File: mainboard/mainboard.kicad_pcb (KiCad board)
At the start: 2 copper layers, 3 parts, among them J1 USB_B_Micro, U1 SX1276, U3 ATtiny85V-10M

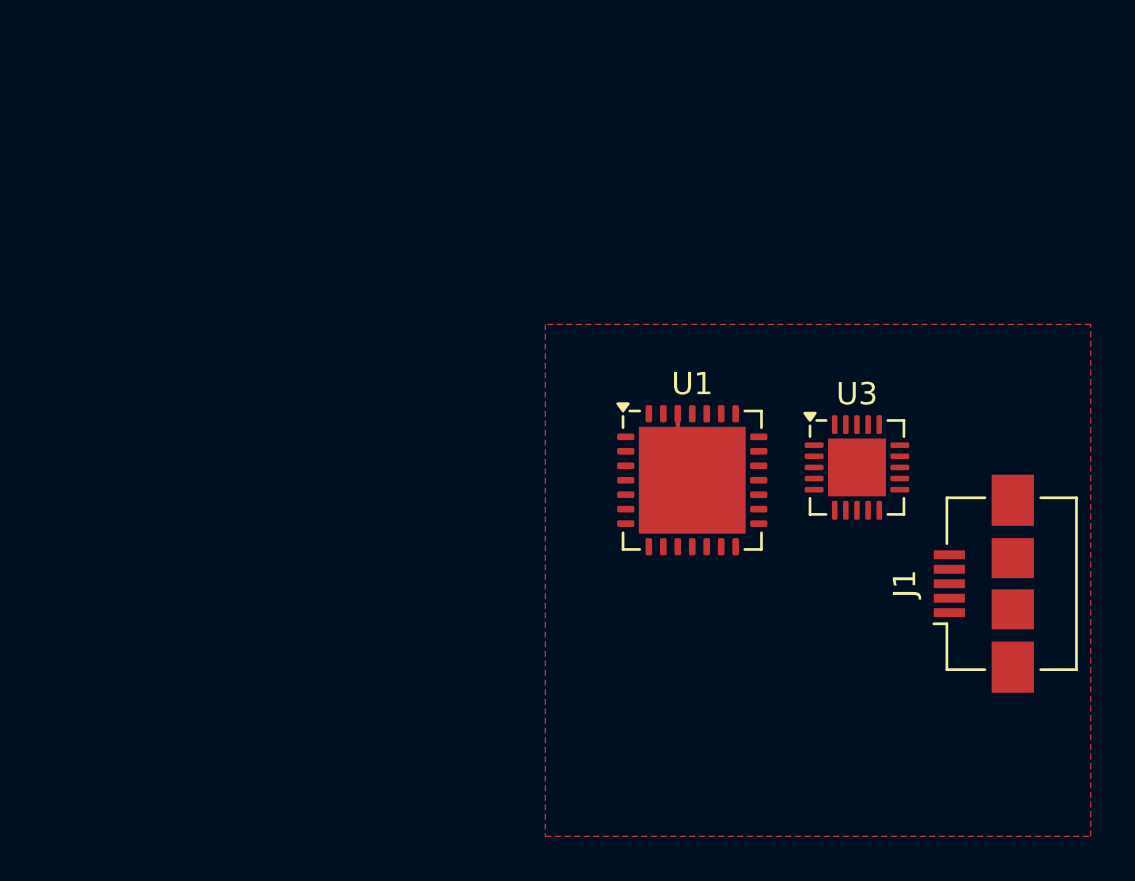
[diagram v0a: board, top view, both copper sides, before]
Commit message: Updated mainboard, and schematics.
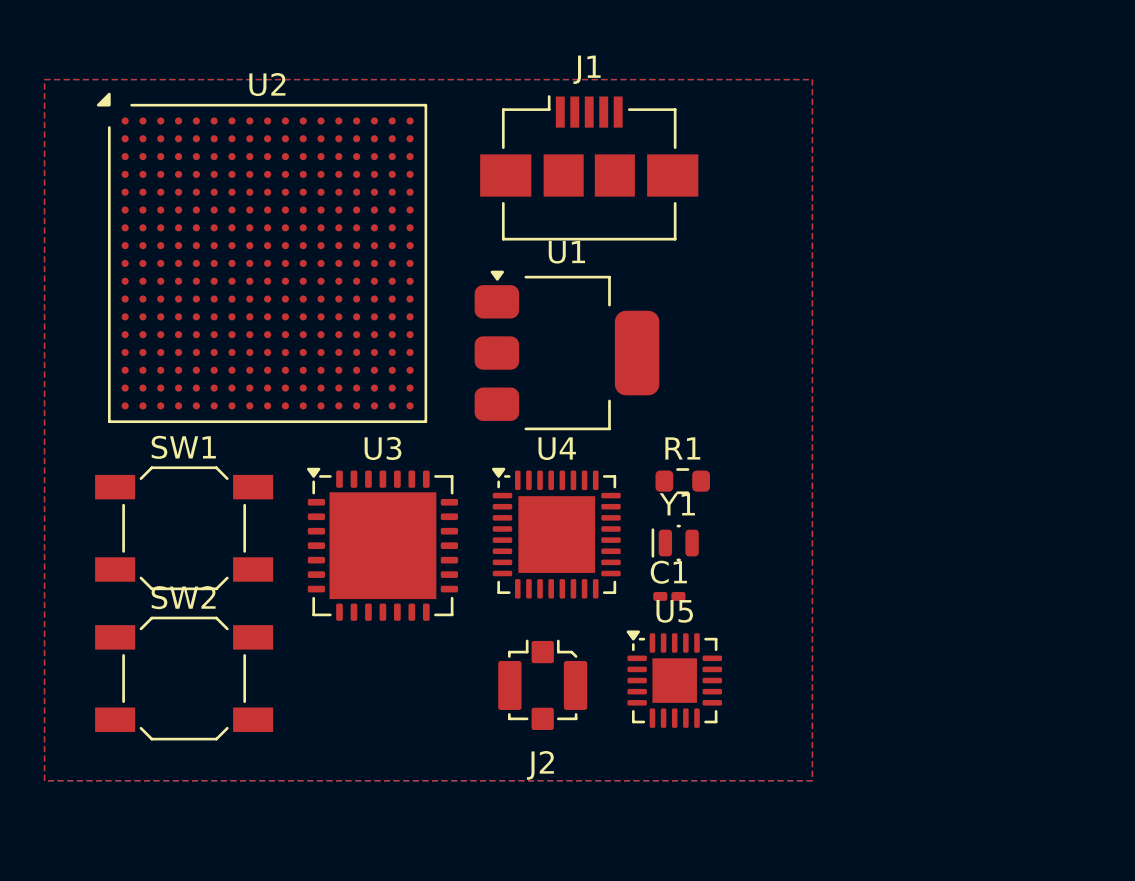
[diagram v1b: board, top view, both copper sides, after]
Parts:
- added C1: 20pF, Capacitor_SMD:C_0201_0603Metric_Pad0.64x0.40mm_HandSolder, F.Cu at (148.6, 57.7)
- added J2: Conn_Coaxial_Small, Connector_Coaxial:U.FL_Molex_MCRF_73412-0110_Vertical, F.Cu at (142.9, 61.7)
- added R1: R, Resistor_SMD:R_0603_1608Metric, F.Cu at (149.2, 52.5)
- added SW1: SW_Push, Button_Switch_SMD:SW_SPST_SKQG_WithoutStem, F.Cu at (126.8, 54.7)
- added SW2: SW_Push, Button_Switch_SMD:SW_SPST_SKQG_WithoutStem, F.Cu at (126.8, 61.4)
- added U2: STM32MP131AAEx, Package_BGA:LFBGA-289_14x14mm_Layout17x17_P0.8mm, F.Cu at (130.5, 42.8)
- added U4: nRF8001, Package_DFN_QFN:QFN-32-1EP_5x5mm_P0.5mm_EP3.45x3.45mm, F.Cu at (143.5, 54.9)
- added U5: BQ25570, Package_DFN_QFN:QFN-20-1EP_3.5x3.5mm_P0.5mm_EP2x2mm, F.Cu at (148.8, 61.5)
- added Y1: Crystal_Small, Crystal:Crystal_SMD_MicroCrystal_CM9V-T1A-2Pin_1.6x1.0mm, F.Cu at (149.0, 55.3)
- U1: value SX1276 -> AMS1117-3.3; footprint Package_DFN_QFN:QFN-28-1EP_6x6mm_P0.65mm_EP4.8x4.8mm -> Package_TO_SOT_SMD:SOT-223-3_TabPin2
- U3: value ATtiny85V-10M -> SX1276; footprint Package_DFN_QFN:QFN-20-1EP_4x4mm_P0.5mm_EP2.6x2.6mm -> Package_DFN_QFN:QFN-28-1EP_6x6mm_P0.65mm_EP4.8x4.8mm
- moved J1 26.5 mm to (145.0, 37.5), turned to 0 degrees
- moved U3 21.6 mm to (135.7, 55.4)
- moved U1 8.02 mm to (144.0, 46.8)
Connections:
- J1 pad 1: unconnected-(J1-VBUS-Pad1) -> Net-(J1-VBUS)
- U1 pad 1: unconnected-(U1-RFI_LF-Pad1) -> Net-(J1-GND)
- U1 pad 2: unconnected-(U1-VR_ANA-Pad2) -> Net-(U1-VO)
- U1 pad 3: unconnected-(U1-VBAT_ANA-Pad3) -> Net-(J1-GND)
- U3 pad 15: unconnected-(U3-VCC-Pad15) -> Net-(J1-GND)
- U3 pad 20: unconnected-(U3-NC-Pad20) -> Net-(J2-In)
- U3 pad 21: Net-(J1-GND) -> unconnected-(U3-RFI_HF-Pad21)
- U3 pad 5: unconnected-(U3-XTAL2/PB4-Pad5) -> Net-(U3-XTA)
- U3 pad 6: unconnected-(U3-NC-Pad6) -> Net-(U3-XTB)
- U3 pad 7: unconnected-(U3-NC-Pad7) -> Net-(U3-~{RESET})
- U3 pad 8: Net-(J1-GND) -> unconnected-(U3-DIO0-Pad8)
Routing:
- net Net-(J1-GND): track 6.01 -> 0.00 mm
- added copper zone on B.Cu, net (none)

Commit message: Update schematic
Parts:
- removed C1: 20pF, Capacitor_SMD:C_0201_0603Metric_Pad0.64x0.40mm_HandSolder
- removed J1: USB_B_Micro, Connector_USB:USB_Micro-B_Amphenol_10104110_Horizontal
- removed J2: Conn_Coaxial_Small, Connector_Coaxial:U.FL_Molex_MCRF_73412-0110_Vertical
- removed R1: R, Resistor_SMD:R_0603_1608Metric
- removed SW1, SW2: SW_Push, Button_Switch_SMD:SW_SPST_SKQG_WithoutStem
- removed U1: AMS1117-3.3, Package_TO_SOT_SMD:SOT-223-3_TabPin2
- removed U2: STM32MP131AAEx, Package_BGA:LFBGA-289_14x14mm_Layout17x17_P0.8mm
- removed U3: SX1276, Package_DFN_QFN:QFN-28-1EP_6x6mm_P0.65mm_EP4.8x4.8mm
- removed U4: nRF8001, Package_DFN_QFN:QFN-32-1EP_5x5mm_P0.5mm_EP3.45x3.45mm
- removed U5: BQ25570, Package_DFN_QFN:QFN-20-1EP_3.5x3.5mm_P0.5mm_EP2x2mm
- removed Y1: Crystal_Small, Crystal:Crystal_SMD_MicroCrystal_CM9V-T1A-2Pin_1.6x1.0mm

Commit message: Added Proof-Of-Concept
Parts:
- added C1: 20pF, Capacitor_SMD:C_0201_0603Metric_Pad0.64x0.40mm_HandSolder, F.Cu at (137.1, 61.0)
- added C1: 20pF, Capacitor_SMD:C_0201_0603Metric_Pad0.64x0.40mm_HandSolder, F.Cu at (169.1, 61.0)
- added C1: 20pF, Capacitor_SMD:C_0201_0603Metric_Pad0.64x0.40mm_HandSolder, F.Cu at (135.6, 95.0)
- added C1: 20pF, Capacitor_SMD:C_0201_0603Metric_Pad0.64x0.40mm_HandSolder, F.Cu at (201.1, 61.0)
- added C1: 20pF, Capacitor_SMD:C_0201_0603Metric_Pad0.64x0.40mm_HandSolder, F.Cu at (167.6, 95.0)
- added C1: 20pF, Capacitor_SMD:C_0201_0603Metric_Pad0.64x0.40mm_HandSolder, F.Cu at (199.6, 95.0)
- added C2: 20pF, Capacitor_SMD:C_0201_0603Metric_Pad0.64x0.40mm_HandSolder, F.Cu at (201.1, 62.7)
- added C2: 20pF, Capacitor_SMD:C_0201_0603Metric_Pad0.64x0.40mm_HandSolder, F.Cu at (167.6, 96.7)
- added C2: 20pF, Capacitor_SMD:C_0201_0603Metric_Pad0.64x0.40mm_HandSolder, F.Cu at (135.6, 96.7)
- added C2: 20pF, Capacitor_SMD:C_0201_0603Metric_Pad0.64x0.40mm_HandSolder, F.Cu at (199.6, 96.7)
- added C2: 20pF, Capacitor_SMD:C_0201_0603Metric_Pad0.64x0.40mm_HandSolder, F.Cu at (169.1, 62.7)
- added C2: 20pF, Capacitor_SMD:C_0201_0603Metric_Pad0.64x0.40mm_HandSolder, F.Cu at (137.1, 62.7)
- added C3: 22 uF, Capacitor_SMD:C_01005_0402Metric, F.Cu at (197.2, 64.0)
- added C3: 22 uF, Capacitor_SMD:C_01005_0402Metric, F.Cu at (163.7, 98.0)
- added C3: 22 uF, Capacitor_SMD:C_01005_0402Metric, F.Cu at (131.7, 98.0)
- added C3: 22 uF, Capacitor_SMD:C_01005_0402Metric, F.Cu at (195.7, 98.0)
- added C3: 22 uF, Capacitor_SMD:C_01005_0402Metric, F.Cu at (165.2, 64.0)
- added C3: 22 uF, Capacitor_SMD:C_01005_0402Metric, F.Cu at (133.2, 64.0)
- added J1: USB_B_Micro, Connector_USB:USB_Micro-B_Amphenol_10104110_Horizontal, F.Cu at (209.5, 38.0)
- added J1: USB_B_Micro, Connector_USB:USB_Micro-B_Amphenol_10104110_Horizontal, F.Cu at (177.5, 38.0)
- added J1: USB_B_Micro, Connector_USB:USB_Micro-B_Amphenol_10104110_Horizontal, F.Cu at (145.5, 38.0)
- added J1: USB_B_Micro, Connector_USB:USB_Micro-B_Amphenol_10104110_Horizontal, F.Cu at (176.0, 72.0)
- added J1: USB_B_Micro, Connector_USB:USB_Micro-B_Amphenol_10104110_Horizontal, F.Cu at (208.0, 72.0)
- added J1: USB_B_Micro, Connector_USB:USB_Micro-B_Amphenol_10104110_Horizontal, F.Cu at (144.0, 72.0)
- added J2: Conn_Coaxial_Small, Connector_Coaxial:U.FL_Molex_MCRF_73412-0110_Vertical, F.Cu at (205.9, 96.2)
- added J2: Conn_Coaxial_Small, Connector_Coaxial:U.FL_Molex_MCRF_73412-0110_Vertical, F.Cu at (173.9, 96.2)
- added J2: Conn_Coaxial_Small, Connector_Coaxial:U.FL_Molex_MCRF_73412-0110_Vertical, F.Cu at (175.4, 62.2)
- added J2: Conn_Coaxial_Small, Connector_Coaxial:U.FL_Molex_MCRF_73412-0110_Vertical, F.Cu at (143.4, 62.2)
- added J2: Conn_Coaxial_Small, Connector_Coaxial:U.FL_Molex_MCRF_73412-0110_Vertical, F.Cu at (141.9, 96.2)
- added J2: Conn_Coaxial_Small, Connector_Coaxial:U.FL_Molex_MCRF_73412-0110_Vertical, F.Cu at (207.4, 62.2)
- added L2: 4.7μH, Inductor_SMD_Wurth:L_Wurth_WE-LQSH-2010, F.Cu at (180.1, 90.0)
- added L2: 4.7μH, Inductor_SMD_Wurth:L_Wurth_WE-LQSH-2010, F.Cu at (212.1, 90.0)
- added L2: 4.7μH, Inductor_SMD_Wurth:L_Wurth_WE-LQSH-2010, F.Cu at (213.6, 56.0)
- added L2: 4.7μH, Inductor_SMD_Wurth:L_Wurth_WE-LQSH-2010, F.Cu at (149.6, 56.0)
- added L2: 4.7μH, Inductor_SMD_Wurth:L_Wurth_WE-LQSH-2010, F.Cu at (181.6, 56.0)
- added L2: 4.7μH, Inductor_SMD_Wurth:L_Wurth_WE-LQSH-2010, F.Cu at (148.1, 90.0)
- added R1: R, Resistor_SMD:R_0603_1608Metric, F.Cu at (212.2, 87.0)
- added R1: R, Resistor_SMD:R_0603_1608Metric, F.Cu at (213.7, 53.0)
- added R1: R, Resistor_SMD:R_0603_1608Metric, F.Cu at (148.2, 87.0)
- added R1: R, Resistor_SMD:R_0603_1608Metric, F.Cu at (180.2, 87.0)
- added R1: R, Resistor_SMD:R_0603_1608Metric, F.Cu at (181.7, 53.0)
- added R1: R, Resistor_SMD:R_0603_1608Metric, F.Cu at (149.7, 53.0)
- added SW2: SW_Push, Button_Switch_SMD:SW_SPST_SKQG_WithoutStem, F.Cu at (189.8, 89.2)
- added SW2: SW_Push, Button_Switch_SMD:SW_SPST_SKQG_WithoutStem, F.Cu at (125.8, 89.2)
- added SW2: SW_Push, Button_Switch_SMD:SW_SPST_SKQG_WithoutStem, F.Cu at (159.3, 55.2)
- added SW2: SW_Push, Button_Switch_SMD:SW_SPST_SKQG_WithoutStem, F.Cu at (157.8, 89.2)
- added SW2: SW_Push, Button_Switch_SMD:SW_SPST_SKQG_WithoutStem, F.Cu at (191.3, 55.2)
- added SW2: SW_Push, Button_Switch_SMD:SW_SPST_SKQG_WithoutStem, F.Cu at (127.3, 55.2)
- added U1: AMS1117-3.3, Package_TO_SOT_SMD:SOT-223-3_TabPin2, F.Cu at (143.0, 81.3)
- added U1: AMS1117-3.3, Package_TO_SOT_SMD:SOT-223-3_TabPin2, F.Cu at (207.0, 81.3)
- added U1: AMS1117-3.3, Package_TO_SOT_SMD:SOT-223-3_TabPin2, F.Cu at (208.5, 47.3)
- added U1: AMS1117-3.3, Package_TO_SOT_SMD:SOT-223-3_TabPin2, F.Cu at (144.5, 47.3)
- added U1: AMS1117-3.3, Package_TO_SOT_SMD:SOT-223-3_TabPin2, F.Cu at (176.5, 47.3)
- added U1: AMS1117-3.3, Package_TO_SOT_SMD:SOT-223-3_TabPin2, F.Cu at (175.0, 81.3)
- added U2: STM32MP131AAEx, Package_BGA:LFBGA-289_14x14mm_Layout17x17_P0.8mm, F.Cu at (193.5, 77.3)
- added U2: STM32MP131AAEx, Package_BGA:LFBGA-289_14x14mm_Layout17x17_P0.8mm, F.Cu at (129.5, 77.3)
- added U2: STM32MP131AAEx, Package_BGA:LFBGA-289_14x14mm_Layout17x17_P0.8mm, F.Cu at (161.5, 77.3)
- added U2: STM32MP131AAEx, Package_BGA:LFBGA-289_14x14mm_Layout17x17_P0.8mm, F.Cu at (163.0, 43.3)
- added U2: STM32MP131AAEx, Package_BGA:LFBGA-289_14x14mm_Layout17x17_P0.8mm, F.Cu at (195.0, 43.3)
- added U2: STM32MP131AAEx, Package_BGA:LFBGA-289_14x14mm_Layout17x17_P0.8mm, F.Cu at (131.0, 43.3)
- added U3: SX1276, Package_DFN_QFN:QFN-28-1EP_6x6mm_P0.65mm_EP4.8x4.8mm, F.Cu at (134.7, 89.9)
- added U3: SX1276, Package_DFN_QFN:QFN-28-1EP_6x6mm_P0.65mm_EP4.8x4.8mm, F.Cu at (198.7, 89.9)
- added U3: SX1276, Package_DFN_QFN:QFN-28-1EP_6x6mm_P0.65mm_EP4.8x4.8mm, F.Cu at (136.2, 55.9)
- added U3: SX1276, Package_DFN_QFN:QFN-28-1EP_6x6mm_P0.65mm_EP4.8x4.8mm, F.Cu at (166.7, 89.9)
- added U3: SX1276, Package_DFN_QFN:QFN-28-1EP_6x6mm_P0.65mm_EP4.8x4.8mm, F.Cu at (168.2, 55.9)
- added U3: SX1276, Package_DFN_QFN:QFN-28-1EP_6x6mm_P0.65mm_EP4.8x4.8mm, F.Cu at (200.2, 55.9)
- added U4: nRF8001, Package_DFN_QFN:QFN-32-1EP_5x5mm_P0.5mm_EP3.45x3.45mm, F.Cu at (208.0, 55.4)
- added U4: nRF8001, Package_DFN_QFN:QFN-32-1EP_5x5mm_P0.5mm_EP3.45x3.45mm, F.Cu at (142.5, 89.4)
- added U4: nRF8001, Package_DFN_QFN:QFN-32-1EP_5x5mm_P0.5mm_EP3.45x3.45mm, F.Cu at (206.5, 89.4)
- added U4: nRF8001, Package_DFN_QFN:QFN-32-1EP_5x5mm_P0.5mm_EP3.45x3.45mm, F.Cu at (174.5, 89.4)
- added U4: nRF8001, Package_DFN_QFN:QFN-32-1EP_5x5mm_P0.5mm_EP3.45x3.45mm, F.Cu at (144.0, 55.4)
- added U4: nRF8001, Package_DFN_QFN:QFN-32-1EP_5x5mm_P0.5mm_EP3.45x3.45mm, F.Cu at (176.0, 55.4)
- added U5: BQ25570, Package_DFN_QFN:QFN-20-1EP_3.5x3.5mm_P0.5mm_EP2x2mm, F.Cu at (211.8, 96.0)
- added U5: BQ25570, Package_DFN_QFN:QFN-20-1EP_3.5x3.5mm_P0.5mm_EP2x2mm, F.Cu at (149.3, 62.0)
- added U5: BQ25570, Package_DFN_QFN:QFN-20-1EP_3.5x3.5mm_P0.5mm_EP2x2mm, F.Cu at (147.8, 96.0)
- added U5: BQ25570, Package_DFN_QFN:QFN-20-1EP_3.5x3.5mm_P0.5mm_EP2x2mm, F.Cu at (179.8, 96.0)
- added U5: BQ25570, Package_DFN_QFN:QFN-20-1EP_3.5x3.5mm_P0.5mm_EP2x2mm, F.Cu at (213.3, 62.0)
- added U5: BQ25570, Package_DFN_QFN:QFN-20-1EP_3.5x3.5mm_P0.5mm_EP2x2mm, F.Cu at (181.3, 62.0)
- added U6: AT24CS32-SSHM, Package_SO:SOIC-8_3.9x4.9mm_P1.27mm, F.Cu at (125.2, 95.9)
- added U6: AT24CS32-SSHM, Package_SO:SOIC-8_3.9x4.9mm_P1.27mm, F.Cu at (157.2, 95.9)
- added U6: AT24CS32-SSHM, Package_SO:SOIC-8_3.9x4.9mm_P1.27mm, F.Cu at (126.7, 61.9)
- added U6: AT24CS32-SSHM, Package_SO:SOIC-8_3.9x4.9mm_P1.27mm, F.Cu at (189.2, 95.9)
- added U6: AT24CS32-SSHM, Package_SO:SOIC-8_3.9x4.9mm_P1.27mm, F.Cu at (190.7, 61.9)
- added U6: AT24CS32-SSHM, Package_SO:SOIC-8_3.9x4.9mm_P1.27mm, F.Cu at (158.7, 61.9)
- added Y1: 20 ppm, Crystal:Crystal_SMD_MicroCrystal_CM9V-T1A-2Pin_1.6x1.0mm, F.Cu at (133.9, 61.6)
- added Y1: 20 ppm, Crystal:Crystal_SMD_MicroCrystal_CM9V-T1A-2Pin_1.6x1.0mm, F.Cu at (132.4, 95.6)
- added Y1: 20 ppm, Crystal:Crystal_SMD_MicroCrystal_CM9V-T1A-2Pin_1.6x1.0mm, F.Cu at (197.9, 61.6)
- added Y1: 20 ppm, Crystal:Crystal_SMD_MicroCrystal_CM9V-T1A-2Pin_1.6x1.0mm, F.Cu at (196.4, 95.6)
- added Y1: 20 ppm, Crystal:Crystal_SMD_MicroCrystal_CM9V-T1A-2Pin_1.6x1.0mm, F.Cu at (165.9, 61.6)
- added Y1: 20 ppm, Crystal:Crystal_SMD_MicroCrystal_CM9V-T1A-2Pin_1.6x1.0mm, F.Cu at (164.4, 95.6)
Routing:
- net Net-(BT1--): track 0.00 -> 337.9 mm, vias 0 -> 12
- net Net-(J1-GND): track 0.00 -> 238.5 mm, vias 0 -> 24
- net Net-(U5-VSTOR): track 0.00 -> 207.7 mm, vias 0 -> 24
- net Net-(J1-VBUS): track 0.00 -> 198.0 mm, vias 0 -> 12
- net Net-(U3-XTB): track 0.00 -> 172.3 mm, vias 0 -> 24
- net Net-(U3-XTA): track 0.00 -> 145.6 mm, vias 0 -> 12
- net Net-(C3-Pad2): track 0.00 -> 118.5 mm, vias 0 -> 12
- net Net-(J2-In): track 0.00 -> 71.8 mm, vias 0 -> 12
- net Net-(U3-~{RESET}): track 0.00 -> 56.4 mm
- net Net-(SC1-+): track 0.00 -> 40.3 mm, vias 0 -> 12
- net Net-(U5-LBUCK): track 0.00 -> 26.4 mm
